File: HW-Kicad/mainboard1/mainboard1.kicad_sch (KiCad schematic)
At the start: 11 parts, among them J1 Conn_01x02_Male, J2 Conn_01x02_Male, J3 Conn_01x07_Male, J4 Conn_01x04_Male, J5 Conn_01x04_Male, U1 MCP1700-2802E_TO92, U2 ESP32-WROOM-E

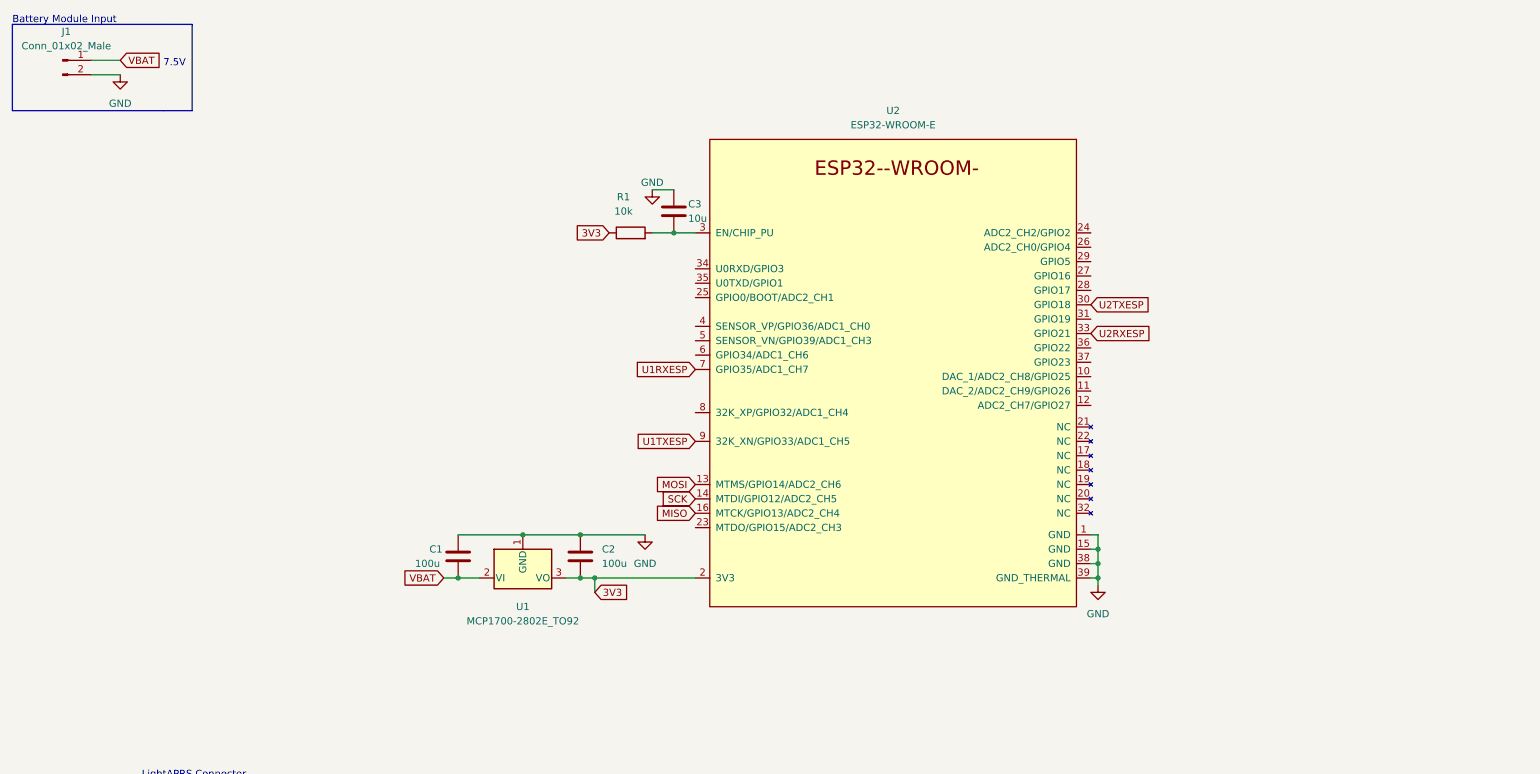
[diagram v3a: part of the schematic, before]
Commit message: agregue circuito de rotura de globo
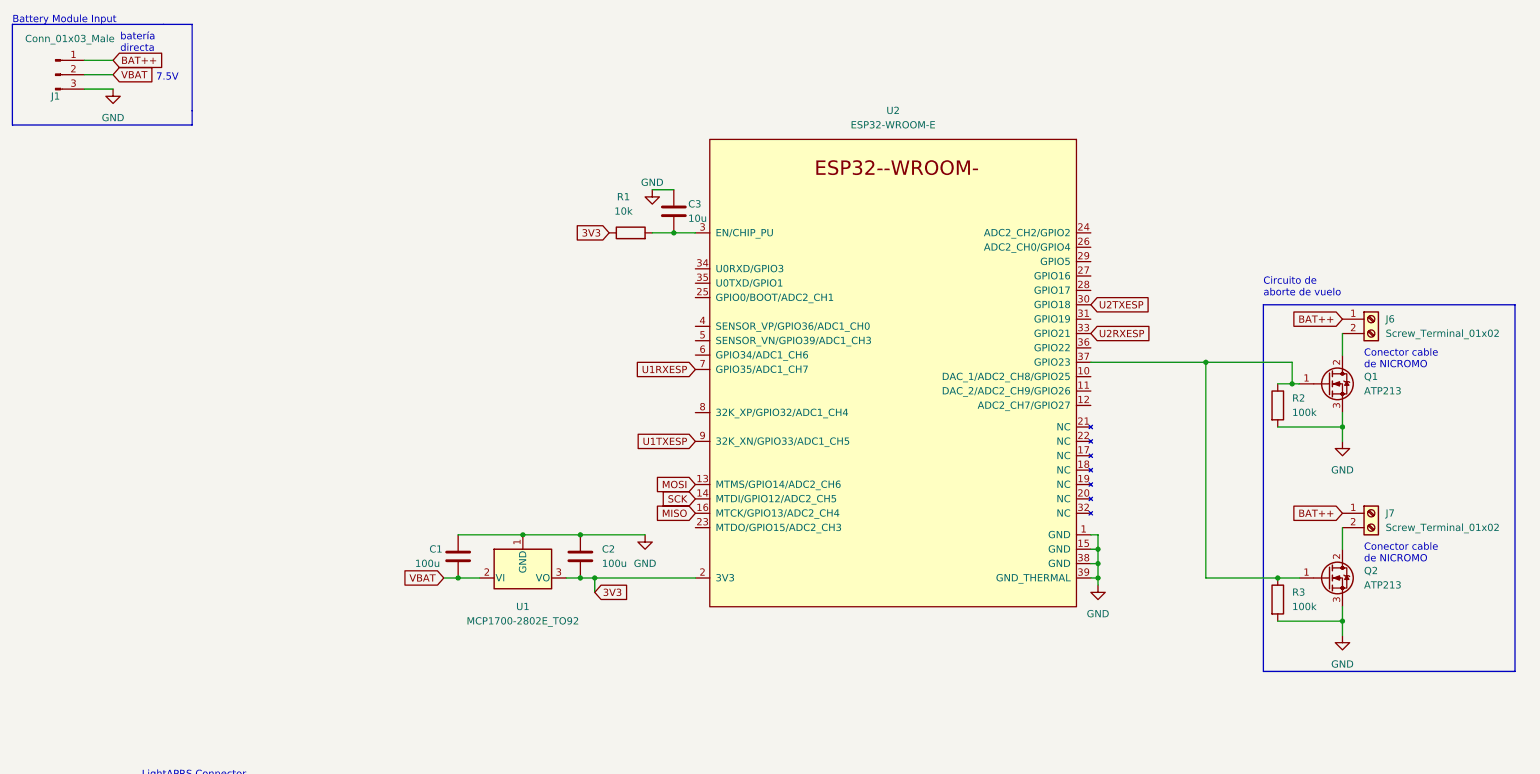
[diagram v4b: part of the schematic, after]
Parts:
- added J6, J7: Screw_Terminal_01x02, TerminalBlock:TerminalBlock_bornier-2_P5.08mm, symbol Connector:Screw_Terminal_01x02
- added Q1, Q2: ATP213, Package_TO_SOT_SMD:TO-252-2, symbol Transistor_FET:STD7NK40Z
- added R2, R3: 100k, Resistor_THT:R_Axial_DIN0207_L6.3mm_D2.5mm_P7.62mm_Horizontal, symbol Device:R
- J1: value Conn_01x02_Male -> Conn_01x03_Male; footprint Connector_Molex:Molex_KK-254_AE-6410-02A_1x02_P2.54mm_Vertical -> Connector_Molex:Molex_KK-254_AE-6410-03A_1x03_P2.54mm_Vertical; symbol Connector:Conn_01x02_Male -> Connector:Conn_01x03_Male
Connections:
- net GND: now also J1.3 (Pin_3), Q1.3 (S), Q2.3 (S), R2.2, R3.2; no longer J1.2 (Pin_2)
- net VBAT: now also J1.2 (Pin_2); no longer J1.1 (Pin_1)
- net at U2.37 (GPIO23): now also Q1.1 (G), Q2.1 (G), R2.1, R3.1
- new net: J6.2 (Pin_2), Q1.2 (D)
- new net: J7.2 (Pin_2), Q2.2 (D)
- new net BAT++: J1.1 (Pin_1), J6.1 (Pin_1), J7.1 (Pin_1)
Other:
- note added: "Circuito de aborte de vuelo"
- note added: "Conector cable de NICROMO"
- note added: "batería directa"

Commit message: cosas en mainboard
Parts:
- added C4: 100uF, Capacitor_THT:CP_Radial_D4.0mm_P2.00mm, symbol Device:C_Polarized
- added J8: Conn_02x10_Odd_Even, Connector_PinSocket_2.00mm:PinSocket_2x10_P2.00mm_Vertical, symbol Connector_Generic:Conn_02x10_Odd_Even
- added U3: Mini360, mini360:Mini360_step-down, symbol mini360:Mini360
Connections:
- net GND: now also U3.1 (IN-)
- net MISO: no longer U2.16 (MTCK/GPIO13/ADC2_CH4)
- net MOSI: no longer U2.13 (MTMS/GPIO14/ADC2_CH6)
- net SCK: no longer U2.14 (MTDI/GPIO12/ADC2_CH5)
- net VBAT: now also U3.2 (IN+)
- new net: C4.1, J8.2 (Pin_2), U3.4 (OUT+)
- new net: C4.2, J8.1 (Pin_1), U3.3 (OUT-)
- new net xtendCTS: J8.9 (Pin_9)
- new net xtendPWR: J8.7 (Pin_7)
- new net xtendRTS: J8.10 (Pin_10)
- new net xtendRX: J8.5 (Pin_5)
- new net xtendTX: J8.6 (Pin_6)
- no-connect marks 1 -> 6
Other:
- note added: "10v"
- note added: "XBEE connector"
- note added: "place as close as possible to connector"
- note added: "set to 5.5"
- note removed: "7.5V"

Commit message: mainboard terminada
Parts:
- removed J6, J7: Screw_Terminal_01x02, TerminalBlock:TerminalBlock_bornier-2_P5.08mm, symbol Connector:Screw_Terminal_01x02
- removed Q1, Q2: ATP213, Package_TO_SOT_SMD:TO-252-2, symbol Transistor_FET:STD7NK40Z
- removed R2, R3: 100k, Resistor_THT:R_Axial_DIN0207_L6.3mm_D2.5mm_P7.62mm_Horizontal, symbol Device:R
- added U4: (no value), symbol lm2596:YAAJ_DCDC_StepDown_LM2596
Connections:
- net BAT++: now also U4.1 (Vin)
- net GND: now also U4.2 (GND), U4.3 (GND)
- net SCL: now also U2.13 (MTMS/GPIO14/ADC2_CH6)
- net SDA: now also U2.11 (DAC_2/ADC2_CH9/GPIO26)
- net VBAT: now also U4.4 (Vout); no longer J1.2 (Pin_2)
- net xtendPWR: now also U2.12 (ADC2_CH7/GPIO27)
- net xtendRX: now also U2.16 (MTCK/GPIO13/ADC2_CH4)
- net xtendTX: now also U2.10 (DAC_1/ADC2_CH8/GPIO25)
- net abortSig: now reaches U2.37 (GPIO23)
- net abortSig: now also J1.2 (Pin_2)
- net MISO: no longer names the net of J3.6 (Pin_6)
- net MOSI: no longer names the net of J3.7 (Pin_7)
- net RST: no longer names the net of J3.2 (Pin_2)
- net SCK: no longer names the net of J3.5 (Pin_5)
- no-connect marks 6 -> 10
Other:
- note added: "Ajustar a 10V"
- note added: "soldar en módulo"
- note removed: "10v"
- note removed: "Circuito de aborte de vuelo"
- note removed: "Conector cable de NICROMO"

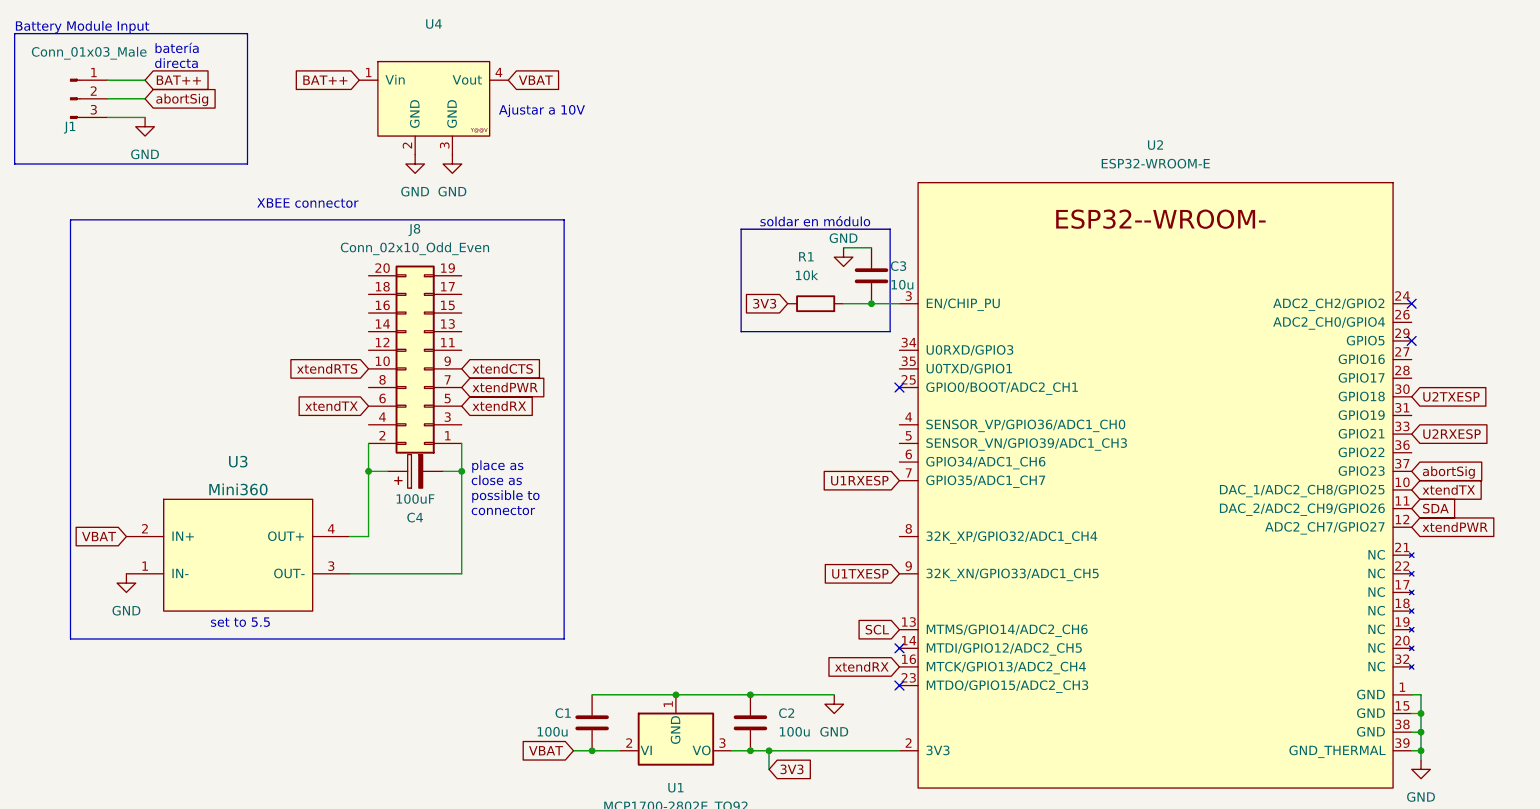
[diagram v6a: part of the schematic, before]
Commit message: actualicé pines del esp32
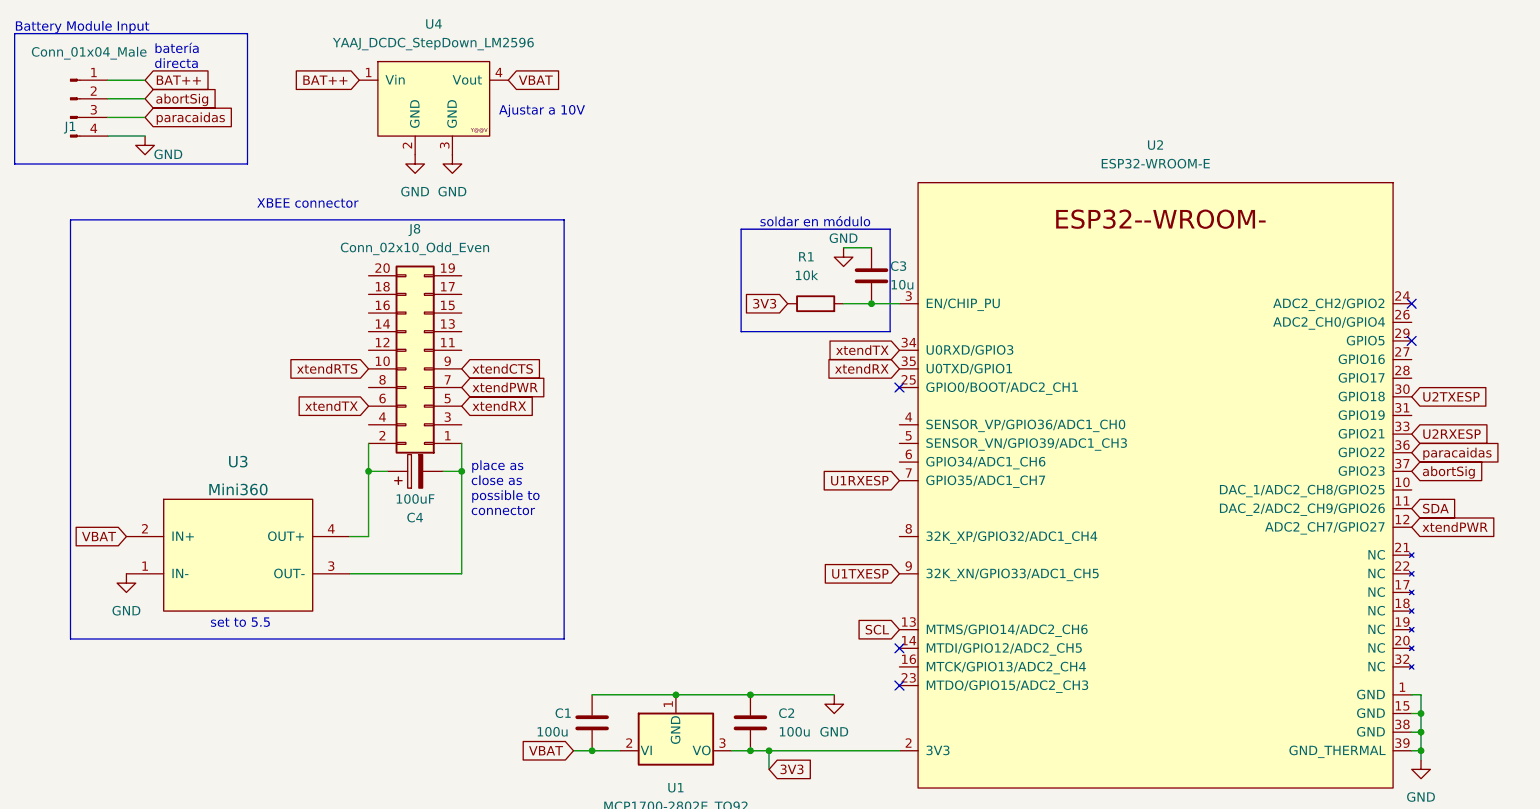
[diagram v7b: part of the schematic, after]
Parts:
- J1: value Conn_01x03_Male -> Conn_01x04_Male; footprint Connector_Molex:Molex_KK-254_AE-6410-03A_1x03_P2.54mm_Vertical -> Connector_Molex:Molex_KK-254_AE-6410-04A_1x04_P2.54mm_Vertical; symbol Connector:Conn_01x03_Male -> Connector:Conn_01x04_Male
- U4: value (none) -> YAAJ_DCDC_StepDown_LM2596; footprint (none) -> lm2596:DC_DC_LM2596_small
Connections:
- net GND: now also J1.4 (Pin_4); no longer J1.3 (Pin_3)
- net xtendRX: now also U2.35 (U0TXD/GPIO1); no longer U2.16 (MTCK/GPIO13/ADC2_CH4)
- net xtendTX: now also U2.34 (U0RXD/GPIO3); no longer U2.10 (DAC_1/ADC2_CH8/GPIO25)
- net paracaidas: now reaches U2.36 (GPIO22)
- net paracaidas: now also J1.3 (Pin_3)
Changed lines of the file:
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@@
+    (stroke (width 0) (type default) (color 0 0 0 0))
+  )
+  (wire (pts (xy 26.67 30.48) (xy 31.75 30.48))
     (stroke (width 0) (type default) (color 0 0 0 0))
   )
@@
     )
   )
+  (global_label "paracaidas" (shape input) (at 31.75 27.94 0) (fields_autoplaced)
+    (effects (font (size 1.27 1.27)) (justify left))
+    (property "Intersheet References" "${INTERSHEET_REFS}" (id 0) (at 44.565 27.8606 0)
+      (effects (font (size 1.27 1.27)) (justify left) hide)
+    )
+  )
   (global_label "PAYLOAD1RX" (shape input) (at 96.52 167.64 0) (fields_autoplaced)
     (effects (font (size 1.27 1.27)) (justify left))
@@
     )
   )
-  (global_label "xtendRX" (shape input) (at 134.62 102.87 180) (fields_autoplaced)
-    (effects (font (size 1.27 1.27)) (justify right))
-    (property "Intersheet References" "${INTERSHEET_REFS}" (id 0) (at 124.5869 102.9494 0)
+  (global_label "xtendRX" (shape input) (at 134.62 62.23 180) (fields_autoplaced)
+    (effects (font (size 1.27 1.27)) (justify right))
+    (property "Intersheet References" "${INTERSHEET_REFS}" (id 0) (at 124.5869 62.3094 0)
       (effects (font (size 1.27 1.27)) (justify right) hide)
     )
@@
     )
   )
-  (global_label "xtendTX" (shape input) (at 204.47 78.74 0) (fields_autoplaced)
-    (effects (font (size 1.27 1.27)) (justify left))
-    (property "Intersheet References" "${INTERSHEET_REFS}" (id 0) (at 214.2007 78.8194 0)
+  (global_label "xtendTX" (shape input) (at 134.62 59.69 180) (fields_autoplaced)
+    (effects (font (size 1.27 1.27)) (justify right))
+    (property "Intersheet References" "${INTERSHEET_REFS}" (id 0) (at 124.8893 59.6106 0)
+      (effects (font (size 1.27 1.27)) (justify right) hide)
+    )
+  )
+  (global_label "paracaidas" (shape input) (at 204.47 73.66 0) (fields_autoplaced)
+    (effects (font (size 1.27 1.27)) (justify left))
+    (property "Intersheet References" "${INTERSHEET_REFS}" (id 0) (at 217.285 73.5806 0)
       (effects (font (size 1.27 1.27)) (justify left) hide)
     )
@@
     (pin "1")
   )
-  (symbol (lib_id "Connector:Conn_01x03_Male") (at 21.59 25.4 0) (unit 1)
+  (symbol (lib_id "Connector:Conn_01x04_Male") (at 21.59 25.4 0) (unit 1)
     (in_bom yes) (on_board yes)
     (property "Reference" "J1" (id 0) (at 21.59 29.21 0))
-    (property "Value" "Conn_01x03_Male" (id 1) (at 24.13 19.05 0))
-    (property "Footprint" "Connector_Molex:Molex_KK-254_AE-6410-03A_1x03_P2.54mm_Vertical" (id 2) (at 21.59 25.4 0)
+    (property "Value" "Conn_01x04_Male" (id 1) (at 24.13 19.05 0))
+    (property "Footprint" "Connector_Molex:Molex_KK-254_AE-6410-04A_1x04_P2.54mm_Vertical" (id 2) (at 21.59 25.4 0)
       (effects (font (size 1.27 1.27)) hide)
     )
@@
     (pin "2")
     (pin "3")
+    (pin "4")
   )
   (symbol (lib_id "Connector:Conn_01x04_Male") (at 88.9 180.34 0) (unit 1)
@@
     (in_bom yes) (on_board yes) (fields_autoplaced)
     (property "Reference" "U4" (id 0) (at 71.12 15.24 0))
-    (property "Value" "" (id 1) (at 71.12 17.78 0))
-    (property "Footprint" "" (id 2) (at 69.85 25.4 0)
+    (property "Value" "YAAJ_DCDC_StepDown_LM2596" (id 1) (at 71.12 17.78 0))
+    (property "Footprint" "lm2596:DC_DC_LM2596_small" (id 2) (at 69.85 25.4 0)
       (effects (font (size 1.27 1.27)) hide)
     )
@@
     (pin "1")
   )
-  (symbol (lib_id "power:GND") (at 31.75 27.94 0) (unit 1)
-    (in_bom yes) (on_board yes) (fields_autoplaced)
-    (property "Reference" "#PWR0101" (id 0) (at 31.75 34.29 0)
-      (effects (font (size 1.27 1.27)) hide)
-    )
-    (property "Value" "GND" (id 1) (at 31.75 33.02 0))
-    (property "Footprint" "" (id 2) (at 31.75 27.94 0)
-      (effects (font (size 1.27 1.27)) hide)
-    )
-    (property "Datasheet" "" (id 3) (at 31.75 27.94 0)
+  (symbol (lib_id "power:GND") (at 31.75 30.48 0) (unit 1)
+    (in_bom yes) (on_board yes)
+    (property "Reference" "#PWR0101" (id 0) (at 31.75 36.83 0)
+      (effects (font (size 1.27 1.27)) hide)
+    )
+    (property "Value" "GND" (id 1) (at 34.925 33.02 0))
+    (property "Footprint" "" (id 2) (at 31.75 30.48 0)
+      (effects (font (size 1.27 1.27)) hide)
+    )
+    (property "Datasheet" "" (id 3) (at 31.75 30.48 0)
       (effects (font (size 1.27 1.27)) hide)
     )
@@
     )
     (path "/33df021e-1bc9-4817-b2c4-40b1726cbd62"
-      (reference "J1") (unit 1) (value "Conn_01x03_Male") (footprint "Connector_Molex:Molex_KK-254_AE-6410-03A_1x03_P2.54mm_Vertical")
+      (reference "J1") (unit 1) (value "Conn_01x04_Male") (footprint "Connector_Molex:Molex_KK-254_AE-6410-04A_1x04_P2.54mm_Vertical")
     )
     (path "/9583fc14-1ded-470d-a1e6-63c816049be6"

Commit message: importe nueva version de leo
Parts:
- removed U3: Mini360, mini360:Mini360_step-down, symbol mini360:Mini360
- added C10, C5, C6, C7, C9: 100n, Capacitor_THT:C_Disc_D3.4mm_W2.1mm_P2.50mm, symbol Device:C
- added C8: 100u, Capacitor_THT:CP_Radial_D6.3mm_P2.50mm, symbol Device:C
- added D1, D2: 1N4148, Diode_THT:D_DO-35_SOD27_P7.62mm_Horizontal, symbol Diode:1N4148
- added F1, F2: Polyfuse, Resistor_THT:R_Axial_DIN0207_L6.3mm_D2.5mm_P5.08mm_Vertical, symbol Device:Polyfuse
- added HS1: Heatsink, Library:9xtend, symbol Mechanical:Heatsink
- added Q1, Q3, Q4, Q6: BC337, Package_TO_SOT_THT:TO-92_Inline_Wide, symbol Transistor_BJT:BC337
- added Q2, Q5: IRF9540N, Package_TO_SOT_THT:TO-220-3_Vertical, symbol Transistor_FET:IRF9540N
- added R10, R11: 4.7k, Resistor_THT:R_Axial_DIN0207_L6.3mm_D2.5mm_P7.62mm_Horizontal, symbol Device:R
- added R12, R13, R16, R18, R19, R20, R22, R24, R8, R9: 10k, Resistor_THT:R_Axial_DIN0207_L6.3mm_D2.5mm_P7.62mm_Horizontal, symbol Device:R
- added R14, R2, R21, R3, R4, R5: 100k, Resistor_THT:R_Axial_DIN0207_L6.3mm_D2.5mm_P7.62mm_Horizontal, symbol Device:R
- added R15, R17, R23, R25: 1, Resistor_THT:R_Axial_DIN0207_L6.3mm_D2.5mm_P7.62mm_Horizontal, symbol Device:R
- added R6, R7: 3.3k, Resistor_THT:R_Axial_DIN0207_L6.3mm_D2.5mm_P7.62mm_Horizontal, symbol Device:R
- added U5: LM7805_TO220, Package_TO_SOT_THT:TO-220-3_Vertical, symbol Regulator_Linear:LM7805_TO220
- added U6: LM324, Package_DIP:DIP-14_W7.62mm, symbol Amplifier_Operational:LM324
- added U7: HEF4093B, Package_DIP:DIP-14_W7.62mm, symbol 4xxx:HEF4093B
- C1, C2: value 100u -> 100n; footprint Capacitor_THT:CP_Radial_D6.3mm_P2.50mm -> Capacitor_THT:C_Disc_D3.4mm_W2.1mm_P2.50mm
- C4: value 100uF -> 470uF; footprint Capacitor_THT:CP_Radial_D4.0mm_P2.00mm -> Capacitor_THT:CP_Radial_D8.0mm_P3.80mm
- U1: footprint Package_TO_SOT_THT:TO-92_Inline -> Package_TO_SOT_THT:TO-92_Inline_Wide
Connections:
- net BAT++: now also C5.1, U5.1 (VI)
- net GND: now also C4.2, J8.1 (Pin_1), C5.2, C6.2, C7.2, C8.2, Q1.3 (E), Q3.3 (E), Q4.3 (E), Q6.3 (E), R15.1, R16.1, R17.2, R22.1, R23.1, R25.2, R8.1, R9.1, U5.2 (GND), U6.11 (V-), U7.7 (GND); no longer J4.4 (Pin_4), J5.4 (Pin_4)
- net VBAT: now also C4.1, J8.2 (Pin_2), F1.1, F2.1; no longer J4.1 (Pin_1), J5.1 (Pin_1)
- net uC_activation_FF1: now reaches U2.27 (GPIO16)
- net uC_activation_FF1: now also D1.2 (A)
- net uC_activation_FF2: now reaches U2.28 (GPIO17)
- net uC_activation_FF2: now also D2.2 (A)
- new net: C9.1, D1.1 (K), R14.1
- new net: C9.2, Q3.2 (B), R14.2, R16.2
- new net: Q1.1 (C), Q2.1 (G), R13.1
- new net: F1.2, Q2.2 (D), R13.2
- new net: C6.1, R2.2, U6.3 (+)
- new net: R11.1, R7.2, R9.2, U6.10 (+)
- new net: C7.1, R3.2, U6.12 (+)
- new net: C10.1, D2.1 (K), R21.1
- new net: C10.2, Q6.2 (B), R21.2, R22.2
- new net: R4.1, U6.2 (-)
- new net: F2.2, Q5.2 (D), R20.2
- new net: Q4.2 (B), R19.2
- new net: U7.13, U7.3
- new net: U7.4, U7.9
- new net: R10.1, R6.2, R8.2, U6.5 (+)
- new net: Q4.1 (C), Q5.1 (G), R20.1
- new net: R5.1, U6.13 (-)
- new net: Q1.2 (B), R12.2
- new net +5V: C8.1, R18.2, R24.2, R6.1, R7.1, U5.3 (VO), U6.4 (V+), U7.14 (VCC)
- new net FF_R1: R10.2, U6.7, U7.6
- new net FF_R2: R11.2, U6.8, U7.2
- new net FF_S1: Q3.1 (C), R18.1, U7.8
- new net FF_S2: Q6.1 (C), R24.1, U7.12
- new net GND_protect_1: J4.4 (Pin_4), R15.2, R17.1, R2.1
- new net GND_protect_2: J5.4 (Pin_4), R23.2, R25.1, R3.1
- new net Q1: R12.1, U7.10, U7.5
- new net Q2: R19.1, U7.1, U7.11
- new net Shunt_out_1: R4.2, U6.1, U6.6 (-)
- new net Shunt_out_2: R5.2, U6.14, U6.9 (-)
- new net VCC_protect_1: J4.1 (Pin_1), Q2.3 (S)
- new net VCC_protect_2: J5.1 (Pin_1), Q5.3 (S)
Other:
- note added: "Ajustar a 5V"
- note removed: "Ajustar a 10V"
- moved on the sheet: C3, C4, J1, J8, R1, U1, U2, U4
